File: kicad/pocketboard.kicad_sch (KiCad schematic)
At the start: 10 parts, among them J1 USB_C_Receptacle_USB2.0_16P

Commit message: Updated to KiCad 9
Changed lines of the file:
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@@
 (kicad_sch
-	(version 20231120)
+	(version 20250114)
 	(generator "eeschema")
-	(generator_version "8.0")
+	(generator_version "9.0")
 	(paper "A4")
 	(title_block
@@
 		(at 163.83 76.2)
 		(size 33.02 31.75)
+		(exclude_from_sim no)
+		(in_bom yes)
+		(on_board yes)
+		(dnp no)
 		(fields_autoplaced yes)
 		(stroke
@@
 		(at 201.93 76.2)
 		(size 27.432 22.86)
+		(exclude_from_sim no)
+		(in_bom yes)
+		(on_board yes)
+		(dnp no)
 		(fields_autoplaced yes)
 		(stroke
@@
 		(at 163.83 116.84)
 		(size 33.02 22.86)
+		(exclude_from_sim no)
+		(in_bom yes)
+		(on_board yes)
+		(dnp no)
 		(stroke
 			(width 0.1524)
@@
 		(at 163.83 64.262)
 		(size 20.32 6.35)
+		(exclude_from_sim no)
+		(in_bom yes)
+		(on_board yes)
+		(dnp no)
 		(fields_autoplaced yes)
 		(stroke
@@
 		)
 	)
+	(embedded_fonts no)
 )

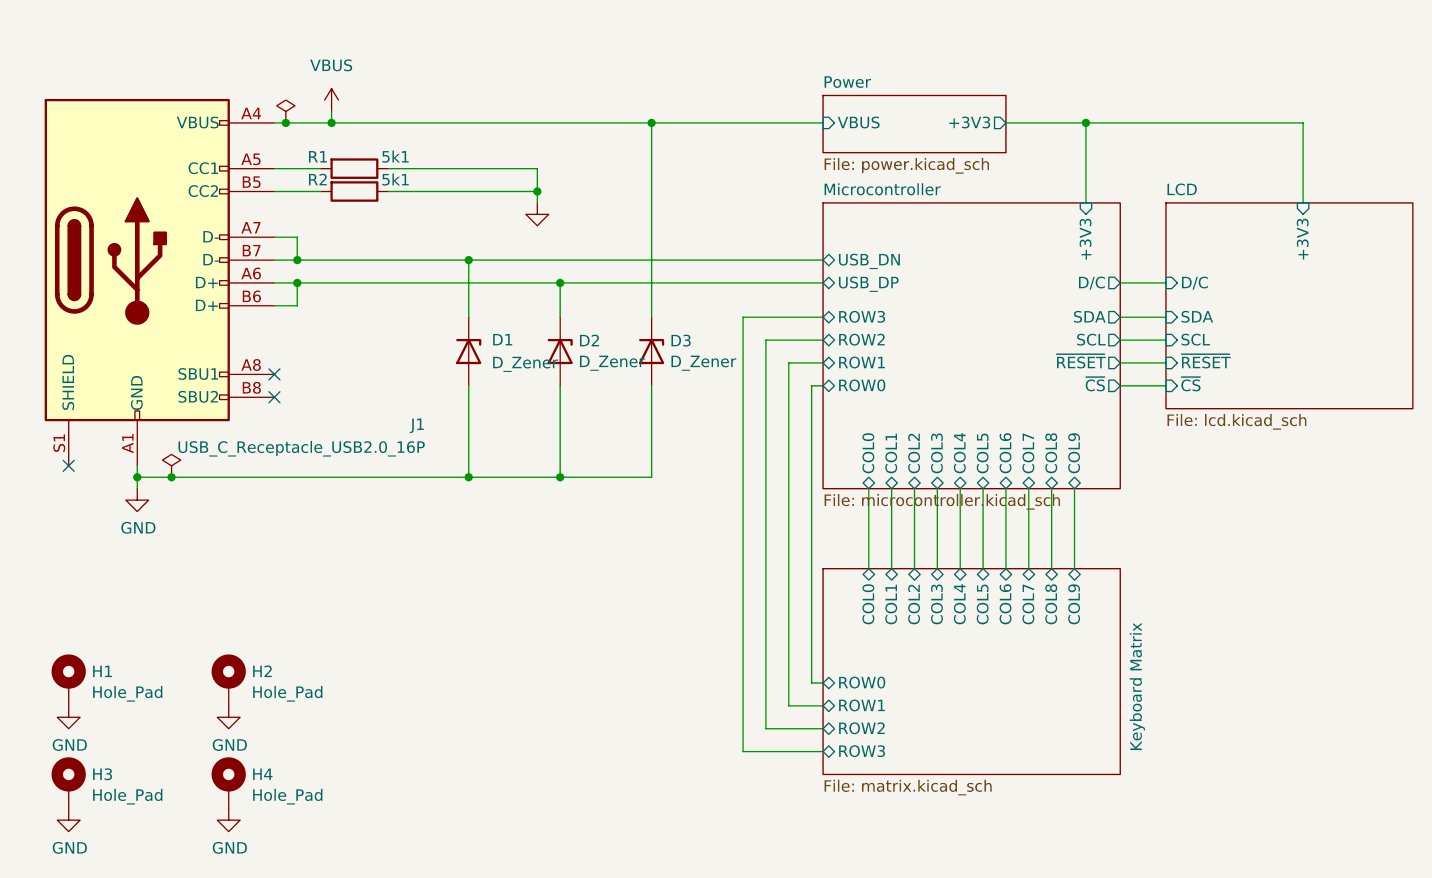
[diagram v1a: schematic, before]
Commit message: changed from rp2040 to nrf
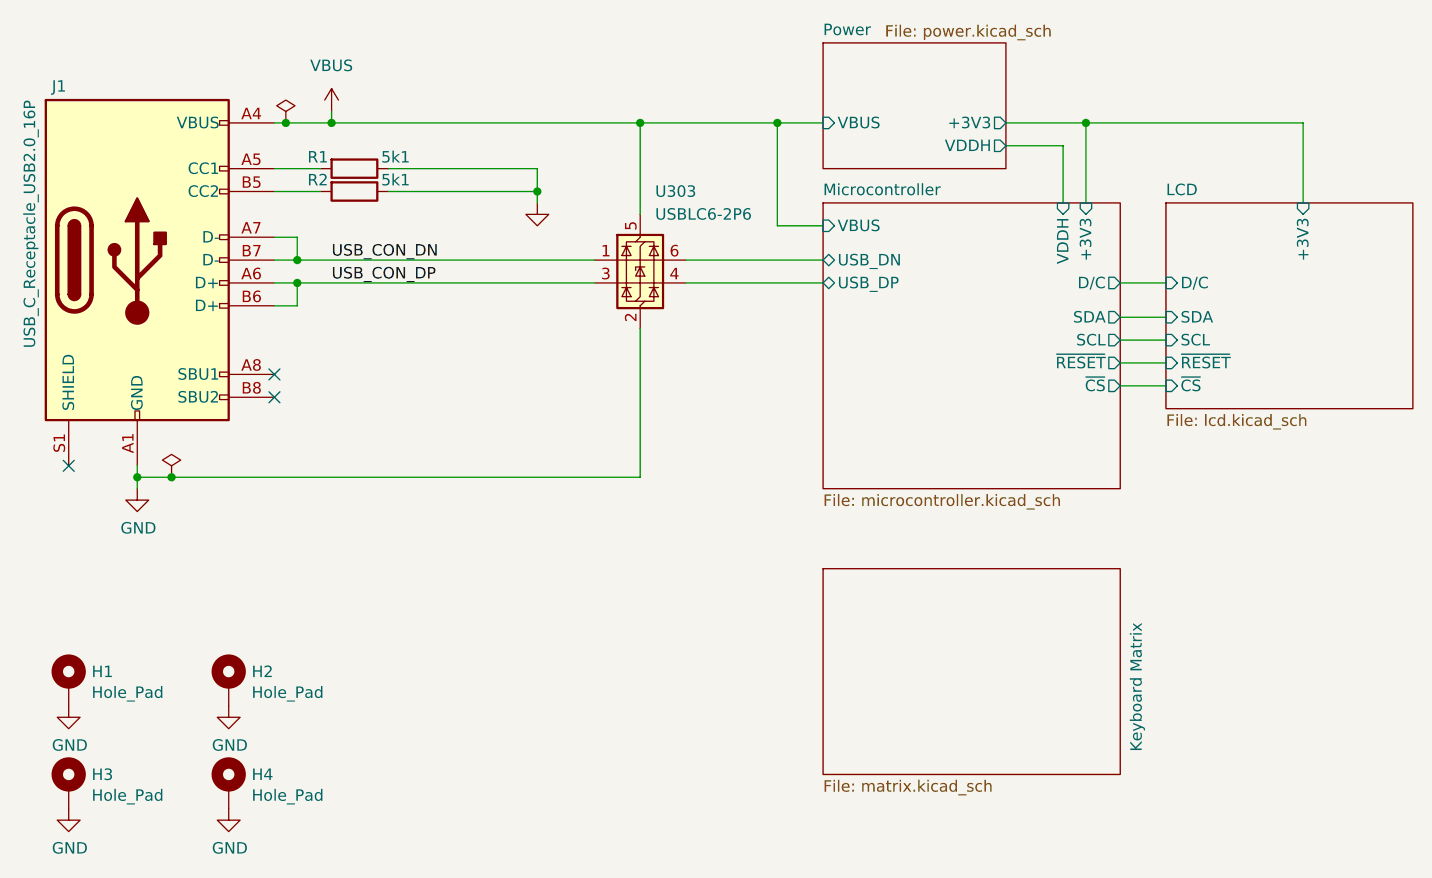
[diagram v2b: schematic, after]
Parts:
- removed D1, D2, D3: D_Zener, Diode_SMD:D_SOD-923, symbol Device:D_Zener
- added U303: USBLC6-2P6, Package_TO_SOT_SMD:SOT-666, symbol Power_Protection:USBLC6-2P6
- R1, R2: footprint Resistor_SMD:R_0603_1608Metric -> Resistor_SMD:R_0402_1005Metric; JLCPCB Part # C23186 -> C25905
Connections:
- net GND: now also U303.2 (GND)
- net Microcontroller/USB_DN: now also U303.6 (I/O1); no longer J1.A7 (D-), J1.B7 (D-)
- net Microcontroller/USB_DP: now also U303.4 (I/O2); no longer J1.A6 (D+), J1.B6 (D+)
- net VBUS: now also U303.5 (VBUS)
- new net USB_CON_DN: J1.A7 (D-), J1.B7 (D-), U303.1 (I/O1)
- new net USB_CON_DP: J1.A6 (D+), J1.B6 (D+), U303.3 (I/O2)
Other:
- sheet Keyboard Matrix ports: added none; removed COL0, COL1, COL2, COL3, COL4, COL5, COL6, COL7, COL8, COL9, ROW0, ROW1, ROW2, ROW3
- sheet Microcontroller ports: added VBUS, VDDH; removed COL0, COL1, COL2, COL3, COL4, COL5, COL6, COL7, COL8, COL9, ROW0, ROW1, ROW2, ROW3
- sheet Power ports: added VDDH; removed none

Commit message: board routed
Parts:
- H1, H2, H3, H4: now not fitted; now left out of the parts list
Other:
- sheet Keyboard Matrix ports: added COL0, COL1, COL2, COL3, COL4, COL5, COL6, COL7, COL8, COL9, P_BTN, ROW0, ROW1, ROW2, ROW3; removed none
- sheet Microcontroller ports: added COL0, COL1, COL2, COL3, COL4, COL5, COL6, COL7, COL8, COL9, P_BTN, ROW0, ROW1, ROW2, ROW3; removed +3V3
